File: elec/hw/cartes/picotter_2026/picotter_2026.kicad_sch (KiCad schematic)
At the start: 0 parts

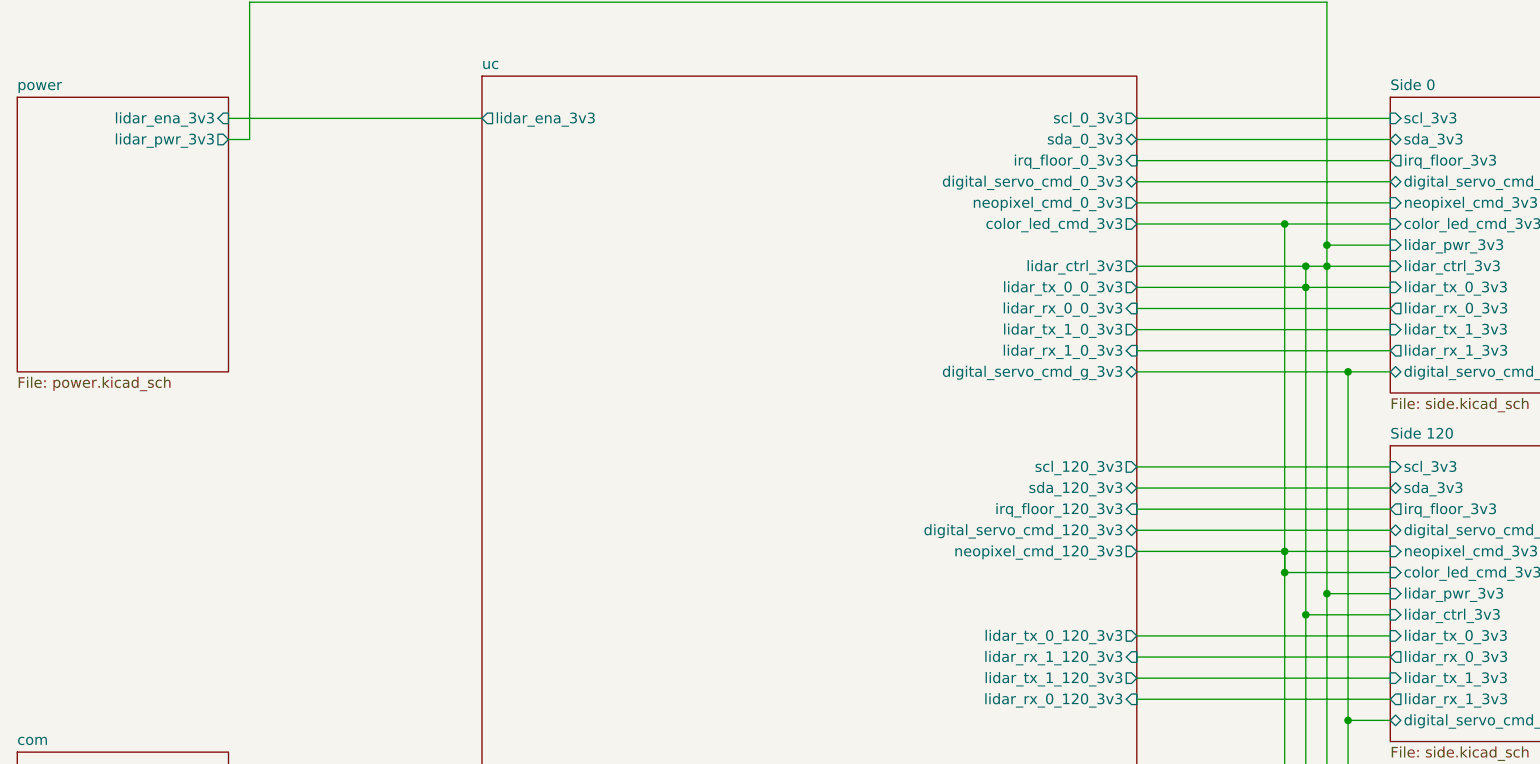
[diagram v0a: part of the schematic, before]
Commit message: pictotter: schematic fixes after review. New prelayout proposition
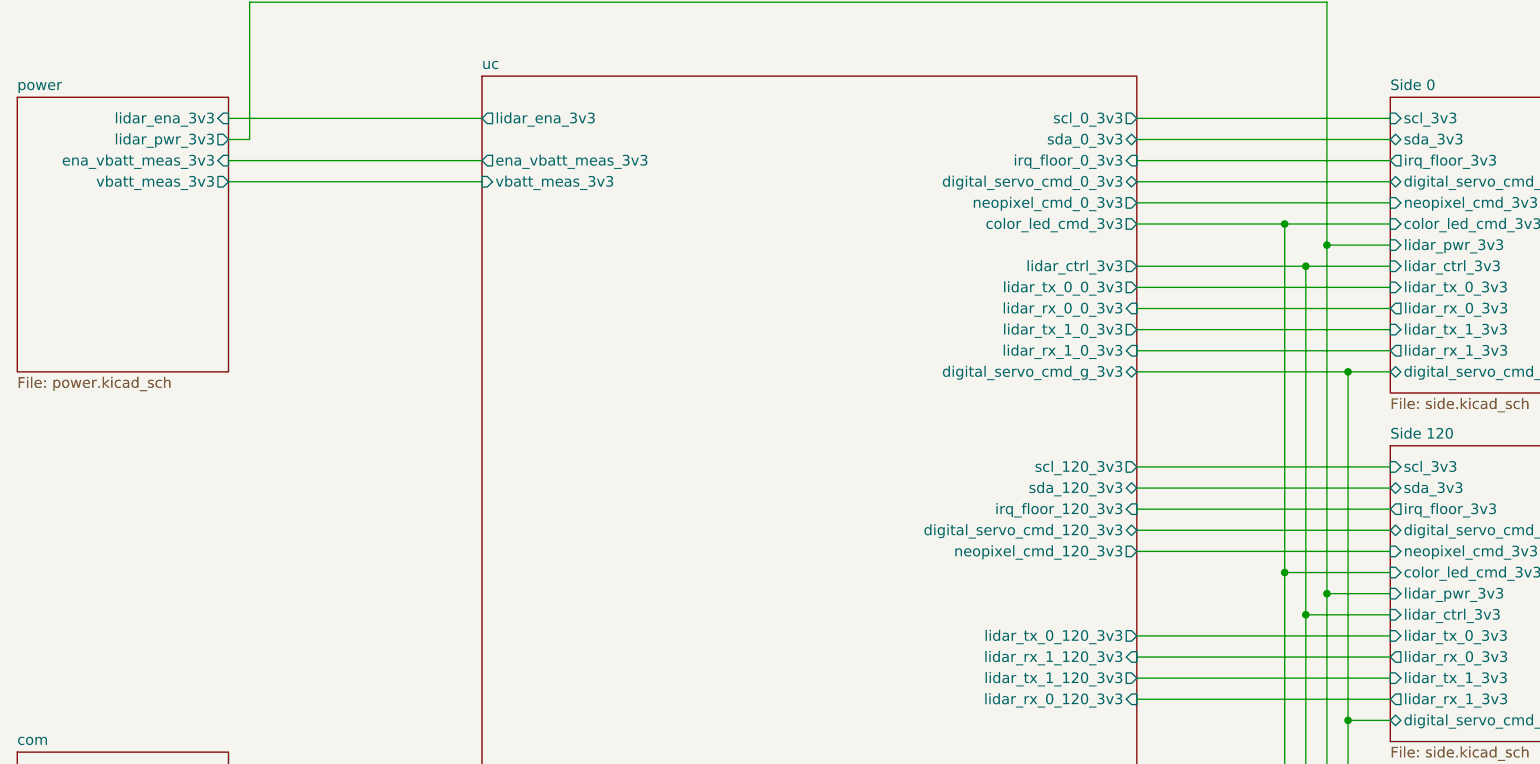
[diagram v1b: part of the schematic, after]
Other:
- sheet power ports: added ena_vbatt_meas_3v3, vbatt_meas_3v3; removed none
- sheet uc ports: added ena_vbatt_meas_3v3, vbatt_meas_3v3; removed none
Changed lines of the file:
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@@
-	)
-	(junction
-		(at 224.79 59.69)
-		(diameter 0)
-		(color 0 0 0 0)
 	)
 	(junction
@@
 		(color 0 0 0 0)
 	)
-	(junction
-		(at 222.25 62.23)
-		(diameter 0)
-		(color 0 0 0 0)
-	)
-	(junction
-		(at 219.71 93.98)
-		(diameter 0)
-		(color 0 0 0 0)
-	)
 	(wire
 		(pts
@@
 	(wire
 		(pts
-			(xy 201.93 93.98) (xy 219.71 93.98)
+			(xy 92.71 49.53) (xy 123.19 49.53)
+		)
+		(stroke
+			(width 0)
+			(type default)
+		)
+	)
+	(wire
+		(pts
+			(xy 201.93 93.98) (xy 232.41 93.98)
 		)
 		(stroke
@@
 	(wire
 		(pts
-			(xy 201.93 62.23) (xy 222.25 62.23)
+			(xy 201.93 62.23) (xy 232.41 62.23)
 		)
 		(stroke
@@
 	(wire
 		(pts
-			(xy 219.71 54.61) (xy 219.71 93.98)
-		)
-		(stroke
-			(width 0)
-			(type default)
-			(color 255 0 255 1)
-		)
-	)
-	(wire
-		(pts
 			(xy 232.41 101.6) (xy 222.25 101.6)
 		)
@@
 	(wire
 		(pts
-			(xy 222.25 101.6) (xy 222.25 62.23)
-		)
-		(stroke
-			(width 0)
-			(type default)
-			(color 255 0 255 1)
-		)
-	)
-	(wire
-		(pts
 			(xy 201.93 64.77) (xy 232.41 64.77)
 		)
@@
 	(wire
 		(pts
-			(xy 224.79 59.69) (xy 232.41 59.69)
+			(xy 222.25 59.69) (xy 232.41 59.69)
 		)
 		(stroke
@@
 	(wire
 		(pts
-			(xy 222.25 59.69) (xy 224.79 59.69)
+			(xy 201.93 52.07) (xy 232.41 52.07)
 		)
 		(stroke
@@
 	(wire
 		(pts
-			(xy 219.71 93.98) (xy 219.71 96.52)
-		)
-		(stroke
-			(width 0)
-			(type default)
-			(color 255 153 0 1)
-		)
-	)
-	(wire
-		(pts
-			(xy 219.71 93.98) (xy 232.41 93.98)
-		)
-		(stroke
-			(width 0)
-			(type default)
-			(color 255 0 255 1)
-		)
-	)
-	(wire
-		(pts
-			(xy 201.93 52.07) (xy 232.41 52.07)
+			(xy 224.79 140.97) (xy 232.41 140.97)
+		)
+		(stroke
+			(width 0)
+			(type default)
+			(color 255 153 0 1)
+		)
+	)
+	(wire
+		(pts
+			(xy 201.93 49.53) (xy 232.41 49.53)
 		)
 		(stroke
@@
 	(wire
 		(pts
-			(xy 224.79 140.97) (xy 232.41 140.97)
-		)
-		(stroke
-			(width 0)
-			(type default)
-			(color 255 153 0 1)
-		)
-	)
-	(wire
-		(pts
-			(xy 201.93 49.53) (xy 232.41 49.53)
+			(xy 201.93 104.14) (xy 232.41 104.14)
+		)
+		(stroke
+			(width 0)
+			(type default)
+			(color 255 0 255 1)
+		)
+	)
+	(wire
+		(pts
+			(xy 201.93 41.91) (xy 232.41 41.91)
 		)
 		(stroke
@@
 	(wire
 		(pts
-			(xy 201.93 104.14) (xy 232.41 104.14)
-		)
-		(stroke
-			(width 0)
-			(type default)
-			(color 255 0 255 1)
-		)
-	)
-	(wire
-		(pts
-			(xy 201.93 41.91) (xy 232.41 41.91)
+			(xy 232.41 114.3) (xy 227.33 114.3)
+		)
+		(stroke
+			(width 0)
+			(type default)
+			(color 255 0 255 1)
+		)
+	)
+	(wire
+		(pts
+			(xy 219.71 54.61) (xy 232.41 54.61)
 		)
 		(stroke
@@
 	(wire
 		(pts
-			(xy 224.79 59.69) (xy 224.79 99.06)
-		)
-		(stroke
-			(width 0)
-			(type default)
-			(color 255 0 255 1)
-		)
-	)
-	(wire
-		(pts
-			(xy 232.41 114.3) (xy 227.33 114.3)
-		)
-		(stroke
-			(width 0)
-			(type default)
-			(color 255 0 255 1)
-		)
-	)
-	(wire
-		(pts
-			(xy 219.71 54.61) (xy 232.41 54.61)
+			(xy 92.71 46.99) (xy 123.19 46.99)
+		)
+		(stroke
+			(width 0)
+			(type default)
+		)
+	)
+	(wire
+		(pts
+			(xy 222.25 59.69) (xy 222.25 101.6)
+		)
+		(stroke
+			(width 0)
+			(type default)
+			(color 255 0 255 1)
+		)
+	)
+	(wire
+		(pts
+			(xy 201.93 133.35) (xy 232.41 133.35)
+		)
+		(stroke
+			(width 0)
+			(type default)
+			(color 255 153 0 1)
+		)
+	)
+	(wire
+		(pts
+			(xy 201.93 72.39) (xy 227.33 72.39)
 		)
 		(stroke
@@
 	(wire
 		(pts
-			(xy 222.25 62.23) (xy 222.25 59.69)
-		)
-		(stroke
-			(width 0)
-			(type default)
-			(color 255 0 255 1)
-		)
-	)
-	(wire
-		(pts
-			(xy 201.93 133.35) (xy 232.41 133.35)
-		)
-		(stroke
-			(width 0)
-			(type default)
-			(color 255 153 0 1)
-		)
-	)
-	(wire
-		(pts
-			(xy 201.93 72.39) (xy 227.33 72.39)
+			(xy 201.93 54.61) (xy 219.71 54.61)
 		)
 		(stroke
@@
 	(wire
 		(pts
-			(xy 201.93 54.61) (xy 219.71 54.61)
+			(xy 201.93 46.99) (xy 232.41 46.99)
 		)
 		(stroke
@@
 	(wire
 		(pts
-			(xy 201.93 46.99) (xy 232.41 46.99)
-		)
-		(stroke
-			(width 0)
-			(type default)
-			(color 0 0 255 1)
-		)
-	)
-	(wire
-		(pts
-			(xy 219.71 96.52) (xy 219.71 93.98)
+			(xy 219.71 54.61) (xy 219.71 96.52)
 		)
 		(stroke
@@
 	(wire
 		(pts
-			(xy 224.79 59.69) (xy 224.79 57.15)
+			(xy 224.79 57.15) (xy 224.79 99.06)
 		)
 		(stroke
@@
 			(type default)
 			(color 255 153 0 1)
-		)
-	)
-	(wire
-		(pts
-			(xy 222.25 62.23) (xy 232.41 62.23)
-		)
-		(stroke
-			(width 0)
-			(type default)
-			(color 0 0 255 1)
 		)
 	)
@@
 			)
 		)
+		(pin "ena_vbatt_meas_3v3" input
+			(at 92.71 46.99 0)
+			(effects
+				(font
+					(size 1.27 1.27)
+				)
+				(justify right)
+			)
+		)
+		(pin "vbatt_meas_3v3" output
+			(at 92.71 49.53 0)
+			(effects
+				(font
+					(size 1.27 1.27)
+				)
+				(justify right)
+			)
+		)
 		(instances
 			(project "picotter_2026"
@@
 			)
 		)
+		(pin "ena_vbatt_meas_3v3" output
+			(at 123.19 46.99 180)
+			(effects
+				(font
+					(size 1.27 1.27)
+				)
+				(justify left)
+			)
+		)
+		(pin "vbatt_meas_3v3" input
+			(at 123.19 49.53 180)
+			(effects
+				(font
+					(size 1.27 1.27)
+				)
+				(justify left)
+			)
+		)

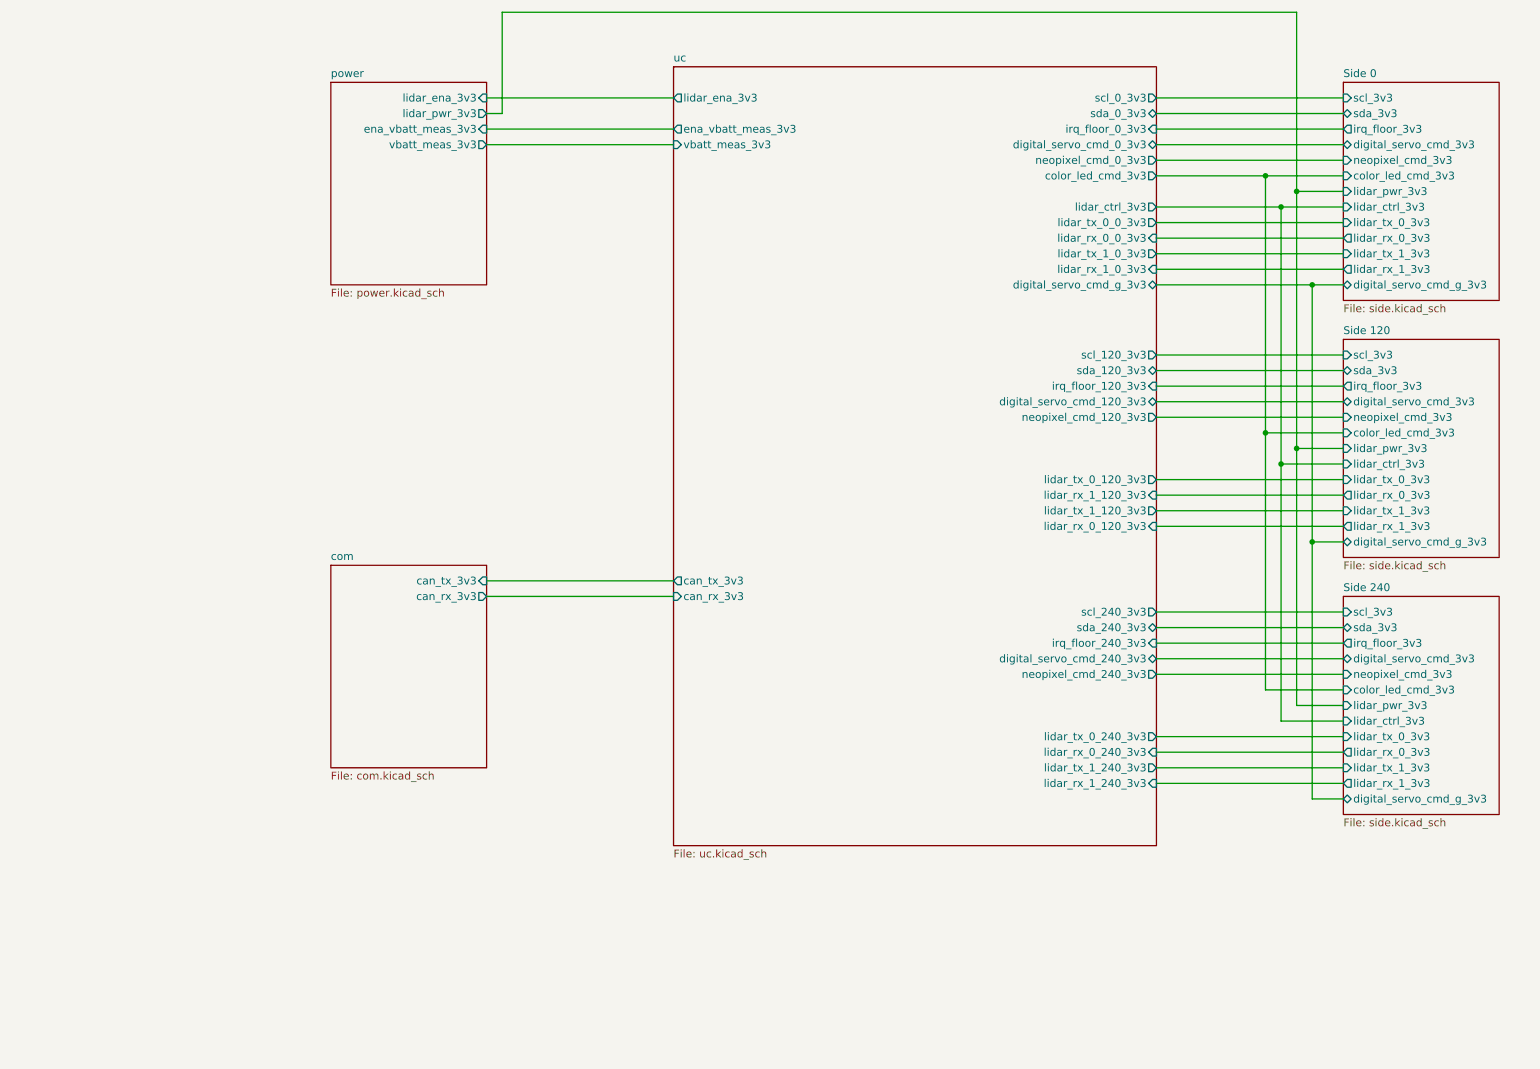
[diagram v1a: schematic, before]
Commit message: picotter: layout almost done (need seriphraphy + layout cleanup)
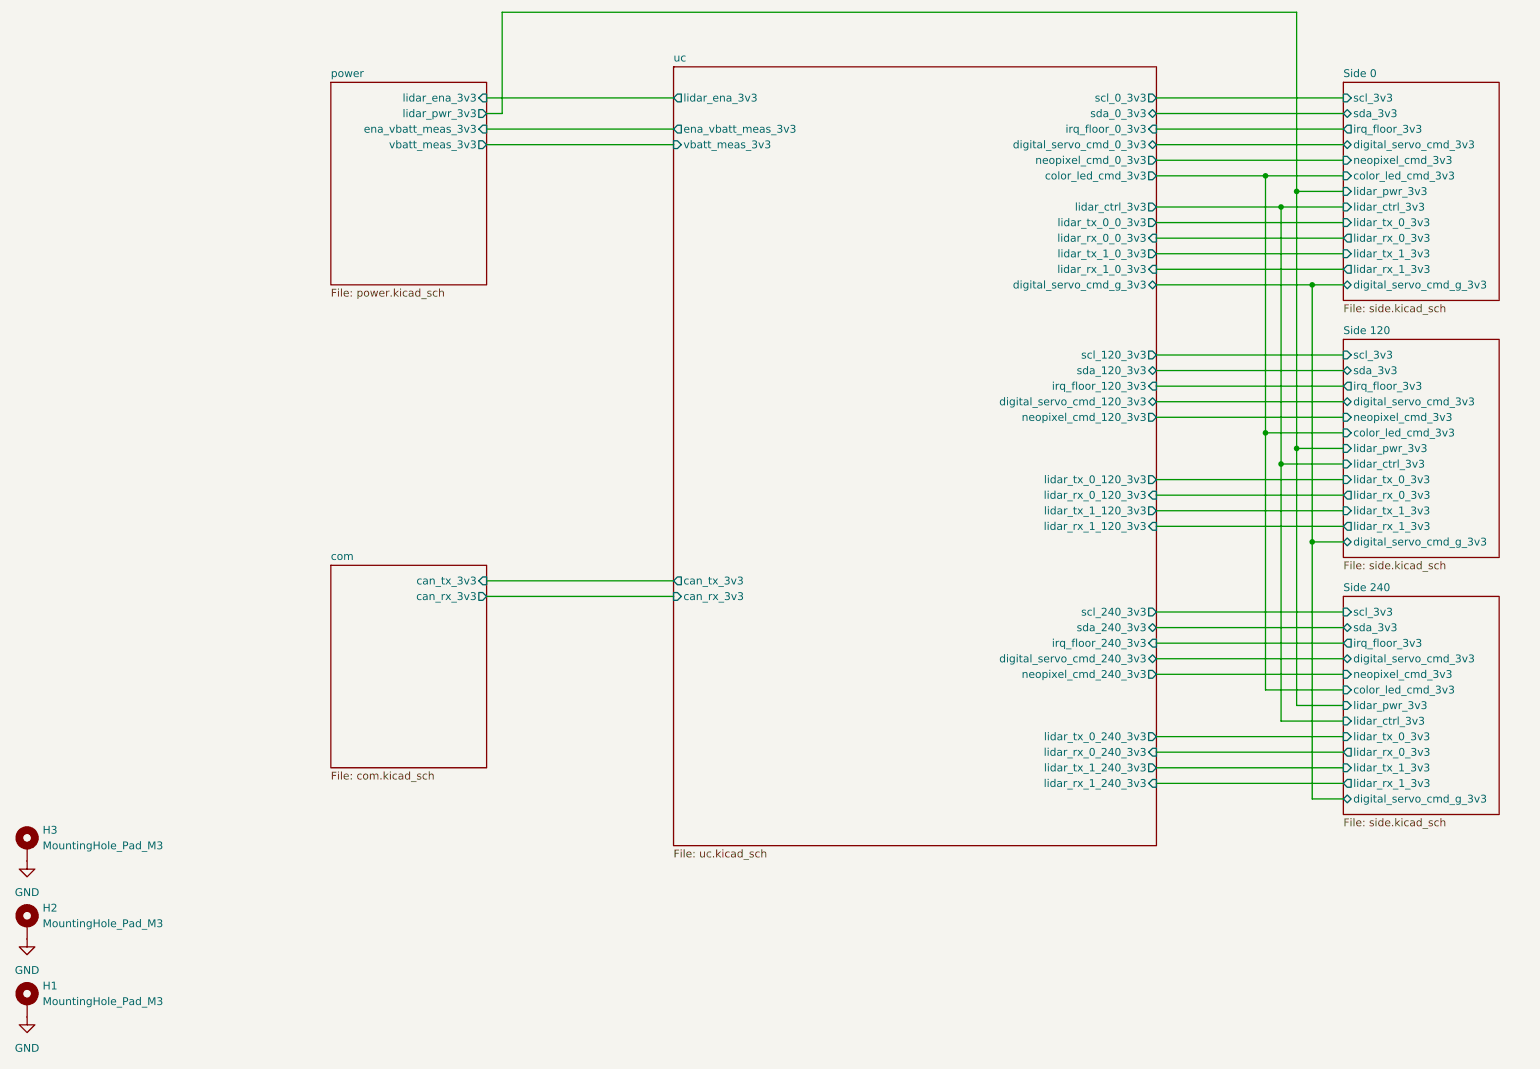
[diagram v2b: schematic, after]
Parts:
- added H1, H2, H3: MountingHole_Pad_M3, cocotter_others:MountingHole_3.2mm_M3_Pad_Via, symbol cocotter_others:MountingHole_Pad_M3
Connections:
- new net GND: H1.1, H2.1, H3.1
